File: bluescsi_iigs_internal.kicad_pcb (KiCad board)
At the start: 2 copper layers, 56.6 x 53.3 mm, 16 parts, among them J1 Conn_02x13_Top_Bottom, J2 Conn_02x13_Top_Bottom, J3 Micro_SD_Card, SW1 SW_SPDT, U1 YAAJ_BluePill, U2 UCC5606, U3 UCC5606

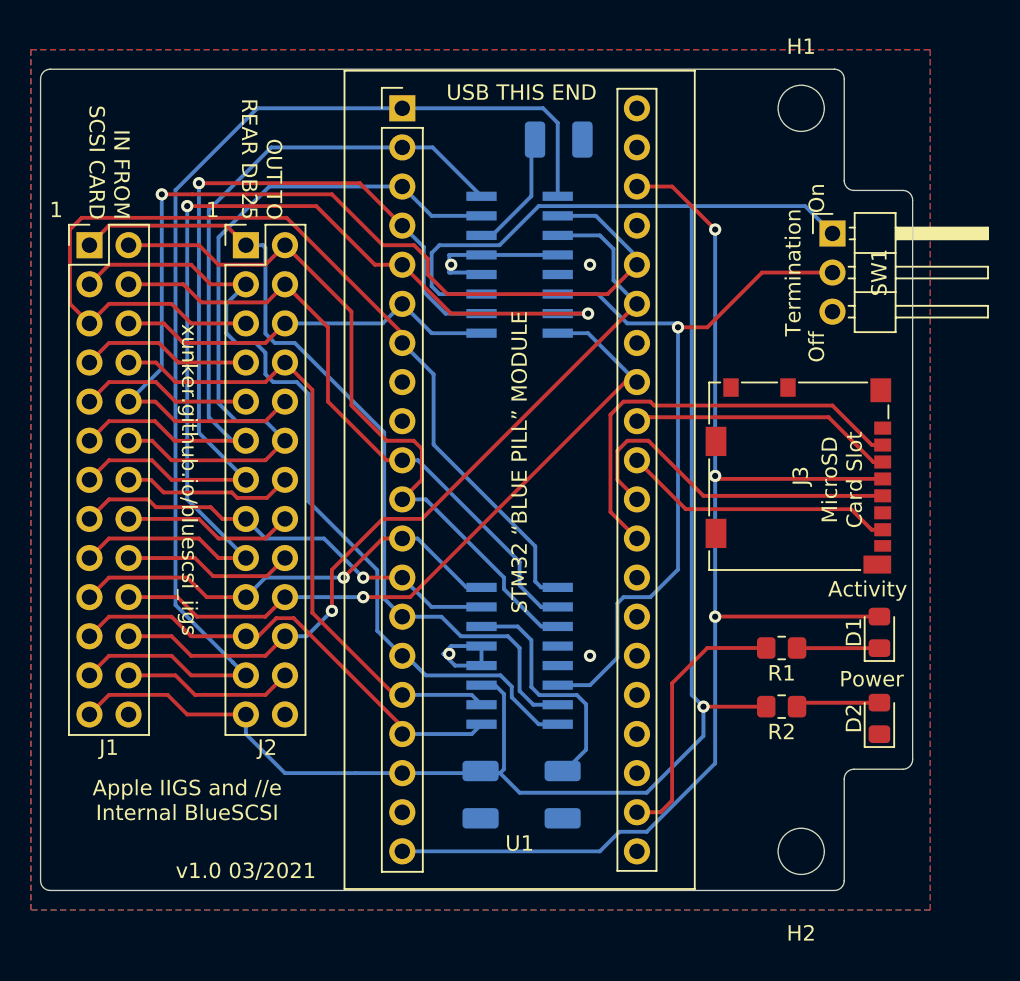
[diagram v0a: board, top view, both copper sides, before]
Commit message: V1.1 from v1.0 Fix IDC26 pin header to be correct! Change capacitor footprint to handsolder variant. Move mounting holes toward centre by about 2.54 and back by 2.54
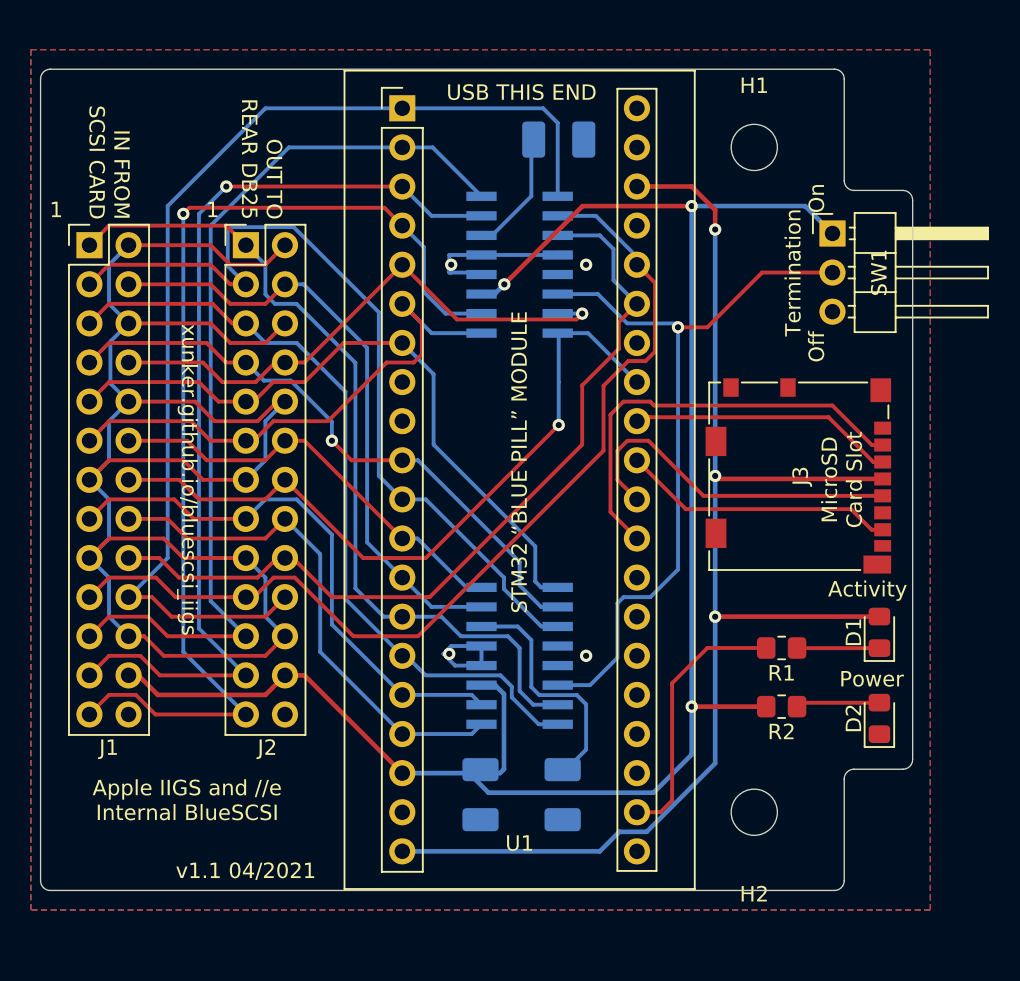
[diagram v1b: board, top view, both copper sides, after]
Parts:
- C1, C2, C3: footprint Capacitor_Tantalum_SMD:CP_EIA-3528-21_Kemet-B -> Capacitor_Tantalum_SMD:CP_EIA-3528-21_Kemet-B_Pad1.50x2.35mm_HandSolder
- J1, J2: value Conn_02x13_Top_Bottom -> Conn_02x13_Odd_Even
- moved H1 3.97 mm to (175.3, 53.3)
- moved H2 3.97 mm to (175.3, 96.5)
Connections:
- J1 pad 10: /SCSI_DB3 -> GND
- J1 pad 11: /SCSI_DB5 -> /SCSI_BSY
- J1 pad 12: /SCSI_DB6 -> /SCSI_SEL
- J1 pad 13: /SCSI_DB7 -> GND
- J1 pad 14: GND -> /SCSI_DBP
- J1 pad 15: /SCSI_C_D -> /SCSI_DB0
- J1 pad 16: GND -> /SCSI_DB1
- J1 pad 17: /SCSI_ATN -> GND
- J1 pad 18: GND -> /SCSI_DB2
- J1 pad 19: /SCSI_SEL -> /SCSI_DB3
- J1 pad 2: /SCSI_MSG -> GND
- J1 pad 20: /SCSI_DBP -> /SCSI_DB4
- J1 pad 21: /SCSI_DB1 -> /SCSI_DB5
- J1 pad 22: /SCSI_DB2 -> GND
- J1 pad 23: /SCSI_DB4 -> /SCSI_DB6
- J1 pad 24: GND -> +5V
- J1 pad 25: +5V -> /SCSI_DB7
- J1 pad 3: /SCSI_I_O -> /SCSI_MSG
- J1 pad 4: /SCSI_RST -> /SCSI_C_D
- J1 pad 5: /SCSI_ACK -> /SCSI_I_O
- J1 pad 6: /SCSI_BSY -> GND
- J1 pad 7: GND -> /SCSI_RST
- J1 pad 8: /SCSI_DB0 -> /SCSI_ATN
- J1 pad 9: GND -> /SCSI_ACK
- J2 pad 10: /SCSI_DB3 -> GND
- J2 pad 11: /SCSI_DB5 -> /SCSI_BSY
- J2 pad 12: /SCSI_DB6 -> /SCSI_SEL
- J2 pad 13: /SCSI_DB7 -> GND
- J2 pad 14: GND -> /SCSI_DBP
- J2 pad 15: /SCSI_C_D -> /SCSI_DB0
- J2 pad 16: GND -> /SCSI_DB1
- J2 pad 17: /SCSI_ATN -> GND
- J2 pad 18: GND -> /SCSI_DB2
- J2 pad 19: /SCSI_SEL -> /SCSI_DB3
- J2 pad 2: /SCSI_MSG -> GND
- J2 pad 20: /SCSI_DBP -> /SCSI_DB4
- J2 pad 21: /SCSI_DB1 -> /SCSI_DB5
- J2 pad 22: /SCSI_DB2 -> GND
- J2 pad 23: /SCSI_DB4 -> /SCSI_DB6
- J2 pad 24: GND -> +5V
- J2 pad 25: +5V -> /SCSI_DB7
- J2 pad 3: /SCSI_I_O -> /SCSI_MSG
- J2 pad 4: /SCSI_RST -> /SCSI_C_D
- J2 pad 5: /SCSI_ACK -> /SCSI_I_O
- J2 pad 6: /SCSI_BSY -> GND
- J2 pad 7: GND -> /SCSI_RST
- J2 pad 8: /SCSI_DB0 -> /SCSI_ATN
- J2 pad 9: GND -> /SCSI_ACK
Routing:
- net GND: track 84.2 -> 127.2 mm
- net /SCSI_ATN: track 67.1 -> 36.9 mm, vias 2 -> 1
- net /SCSI_ACK: track 64.3 -> 44.4 mm
- net /SCSI_DB6: track 46.6 -> 62.3 mm, vias 0 -> 1
- net /SCSI_DB7: track 55.3 -> 69.5 mm
- net /SCSI_DB5: track 48.4 -> 59.8 mm
- net /SCSI_C_D: track 28.9 -> 40.1 mm, vias 1 -> 0
- net +5V: track 126.7 -> 117.2 mm, vias 1 -> 3
- net /SCSI_BSY: track 25.3 -> 34.7 mm
- net /SCSI_MSG: track 46.9 -> 54.2 mm
- net /SCSI_DB4: track 76.8 -> 70.8 mm
- net /SCSI_DB0: track 41.7 -> 36.5 mm
- net /SCSI_DB3: track 67.7 -> 62.9 mm, vias 1 -> 0
- net /SCSI_I_O: track 54.6 -> 50.5 mm
- net /SCSI_DB1: track 30.7 -> 34.2 mm
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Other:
- net class POWER: trace_width 0.25 -> 0.3
- board text added: "v1.1 04/2021"
- board text removed: "v1.0 03/2021"

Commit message: Increase trace size for +3.3v and +5v
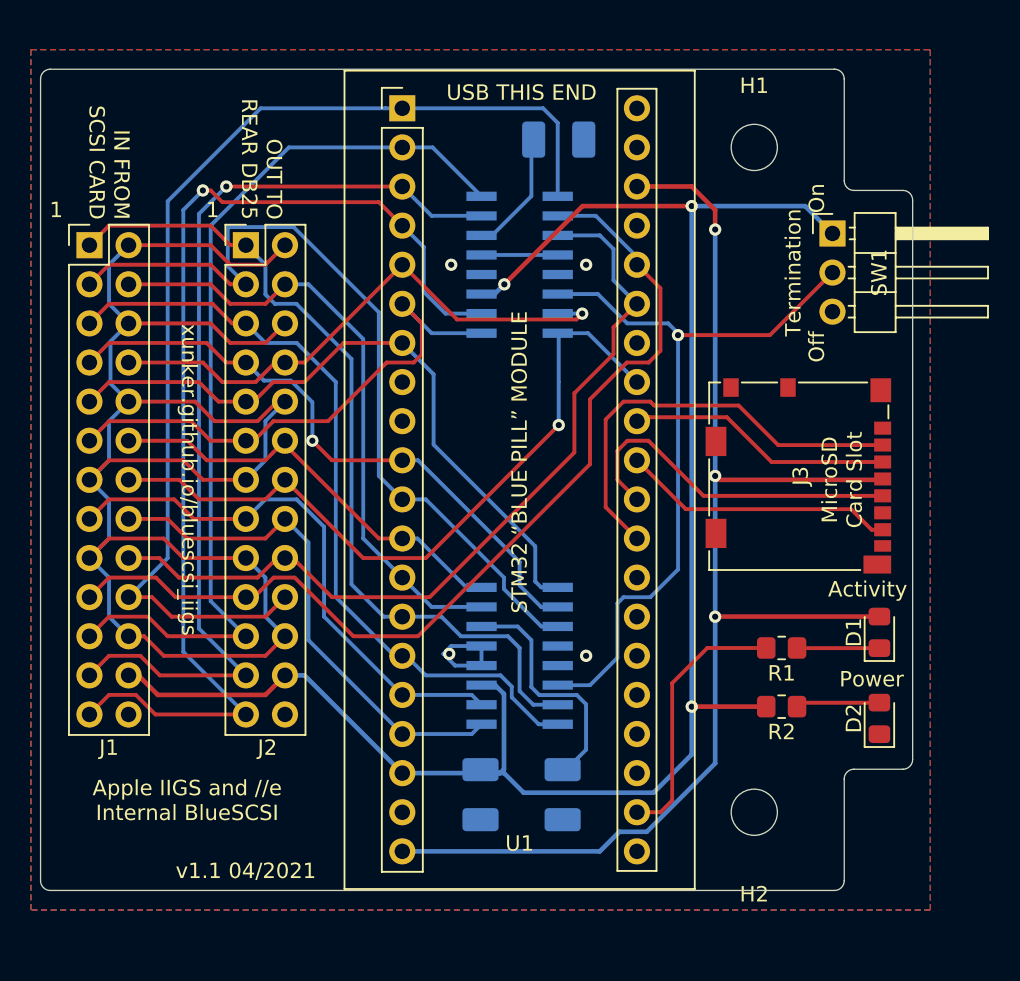
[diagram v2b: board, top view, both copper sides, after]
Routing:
- net GND: track 127.2 -> 122.0 mm
- net /SCSI_DB7: track 69.5 -> 70.6 mm
- net /SCSI_RST: track 39.7 -> 40.4 mm

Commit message: Fix db25 connector wiring
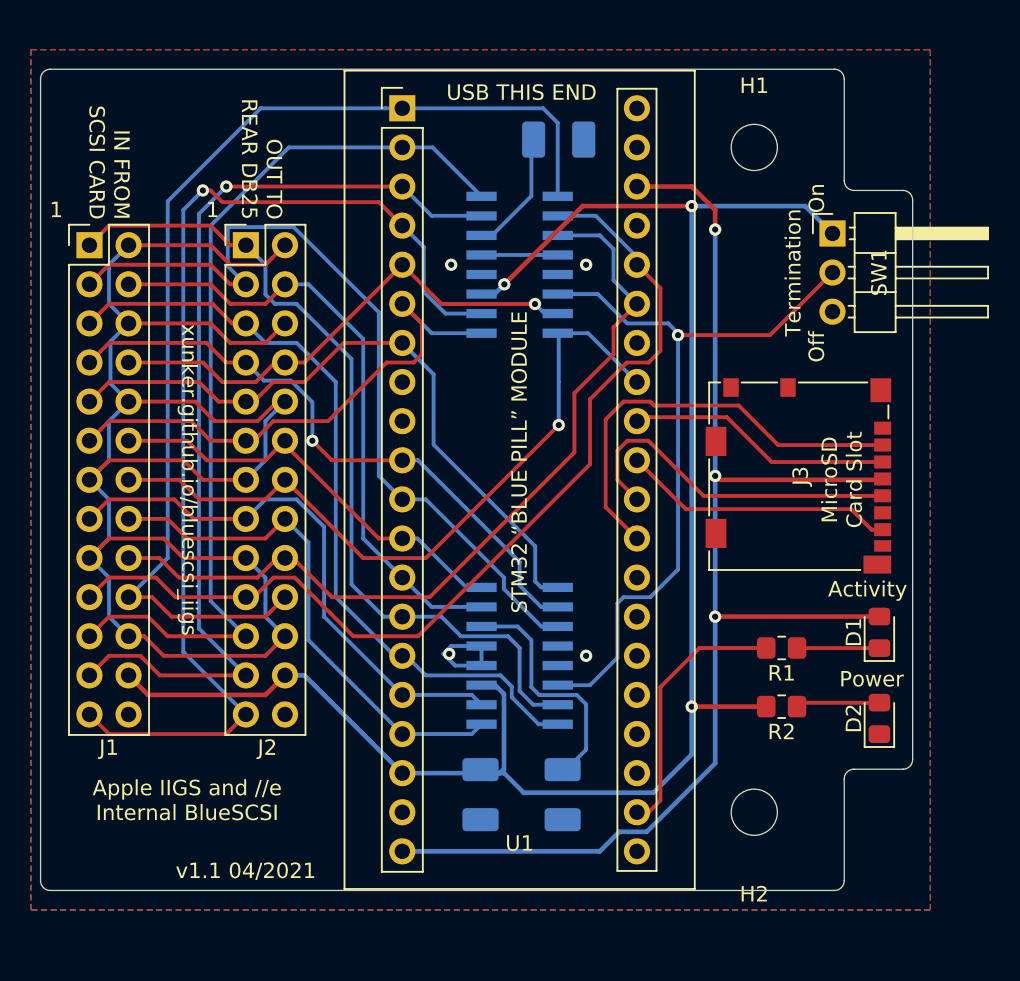
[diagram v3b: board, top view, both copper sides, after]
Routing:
- net /SCSI_ATN: track 36.9 -> 33.4 mm
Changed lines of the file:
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@@
     (thickness 1.6)
     (drawings 46)
-    (tracks 415)
+    (tracks 413)
     (zones 0)
     (modules 16)
@@
   (gr_line (start 180.467 101.6) (end 129.54 101.6) (layer Edge.Cuts) (width 0.05))
   (gr_line (start 185.547 56.769) (end 185.547 93.091) (layer Edge.Cuts) (width 0.05))
-  (segment (start 143.51 88.9) (end 144.78 87.63) (width 0.3) (layer F.Cu) (net 12))
-  (segment (start 135.255 87.63) (end 136.525 88.9) (width 0.3) (layer F.Cu) (net 12))
-  (segment (start 136.525 88.9) (end 143.51 88.9) (width 0.3) (layer F.Cu) (net 12))
-  (segment (start 134.62 87.63) (end 135.255 87.63) (width 0.3) (layer F.Cu) (net 12))
   (segment (start 146.05 87.63) (end 152.4 93.98) (width 0.3) (layer B.Cu) (net 12))
   (segment (start 144.78 87.63) (end 146.05 87.63) (width 0.3) (layer B.Cu) (net 12))
@@
   (via (at 171.196 89.662) (size 0.8) (drill 0.4) (layers F.Cu B.Cu) (net 12))
   (segment (start 176.038 89.662) (end 171.196 89.662) (width 0.3) (layer F.Cu) (net 12))
+  (segment (start 157.545 88.265) (end 158.4265 88.265) (width 0.3) (layer B.Cu) (net 12) (status 30))
+  (segment (start 158.75 93.98) (end 152.4 93.98) (width 0.3) (layer B.Cu) (net 12) (status 20))
+  (segment (start 159.004 93.726) (end 158.75 93.98) (width 0.3) (layer B.Cu) (net 12))
+  (segment (start 159.004 88.8425) (end 159.004 93.726) (width 0.3) (layer B.Cu) (net 12))
+  (segment (start 158.4265 88.265) (end 159.004 88.8425) (width 0.3) (layer B.Cu) (net 12) (status 10))
+  (segment (start 171.196 92.7735) (end 171.196 89.662) (width 0.3) (layer B.Cu) (net 12))
+  (segment (start 168.7195 95.25) (end 171.196 92.7735) (width 0.3) (layer B.Cu) (net 12))
+  (segment (start 160.28075 95.25) (end 168.7195 95.25) (width 0.3) (layer B.Cu) (net 12))
+  (segment (start 158.99725 93.9665) (end 160.28075 95.25) (width 0.3) (layer B.Cu) (net 12))
+  (segment (start 156.718 93.9665) (end 158.99725 93.9665) (width 0.3) (layer B.Cu) (net 12))
+  (segment (start 143.51 88.9) (end 144.78 87.63) (width 0.3) (layer F.Cu) (net 12))
+  (segment (start 135.89 88.9) (end 143.51 88.9) (width 0.3) (layer F.Cu) (net 12))
+  (segment (start 134.62 87.63) (end 135.89 88.9) (width 0.3) (layer F.Cu) (net 12))
   (via (at 155.448 86.233) (size 0.8) (drill 0.4) (layers F.Cu B.Cu) (net 13))
   (segment (start 155.575 85.725) (end 155.067 86.233) (width 0.25) (layer B.Cu) (net 13))
@@
   (segment (start 133.35 63.5) (end 134.62 64.77) (width 0.25) (layer B.Cu) (net 13))
   (segment (start 134.62 59.69) (end 133.35 60.96) (width 0.25) (layer B.Cu) (net 13))
-  (segment (start 157.545 88.265) (end 158.4265 88.265) (width 0.3) (layer B.Cu) (net 12) (status 30))
-  (segment (start 158.75 93.98) (end 152.4 93.98) (width 0.3) (layer B.Cu) (net 12) (status 20))
-  (segment (start 159.004 93.726) (end 158.75 93.98) (width 0.3) (layer B.Cu) (net 12))
-  (segment (start 159.004 88.8425) (end 159.004 93.726) (width 0.3) (layer B.Cu) (net 12))
-  (segment (start 158.4265 88.265) (end 159.004 88.8425) (width 0.3) (layer B.Cu) (net 12) (status 10))
-  (segment (start 171.196 92.7735) (end 171.196 89.662) (width 0.3) (layer B.Cu) (net 12))
-  (segment (start 168.7195 95.25) (end 171.196 92.7735) (width 0.3) (layer B.Cu) (net 12))
-  (segment (start 160.28075 95.25) (end 168.7195 95.25) (width 0.3) (layer B.Cu) (net 12))
-  (segment (start 158.99725 93.9665) (end 160.28075 95.25) (width 0.3) (layer B.Cu) (net 12))
-  (segment (start 156.718 93.9665) (end 158.99725 93.9665) (width 0.3) (layer B.Cu) (net 12))
   (segment (start 162.495 51.751) (end 162.495 56.515) (width 0.25) (layer B.Cu) (net 14) (status 20))
   (segment (start 161.544 50.8) (end 162.495 51.751) (width 0.25) (layer B.Cu) (net 14))
@@
   (segment (start 146.05 67.31) (end 152.4 60.96) (width 0.25) (layer F.Cu) (net 19))
   (segment (start 144.78 67.31) (end 146.05 67.31) (width 0.25) (layer F.Cu) (net 19))
-  (via (at 164.084 64.135) (size 0.8) (drill 0.4) (layers F.Cu B.Cu) (net 19))
-  (segment (start 162.495 64.135) (end 164.084 64.135) (width 0.25) (layer B.Cu) (net 19))
-  (segment (start 163.703 64.516) (end 164.084 64.135) (width 0.25) (layer F.Cu) (net 19))
-  (segment (start 155.956 64.516) (end 163.703 64.516) (width 0.25) (layer F.Cu) (net 19))
-  (segment (start 152.4 60.96) (end 155.956 64.516) (width 0.25) (layer F.Cu) (net 19))
   (segment (start 142.87359 68.58) (end 144.14359 67.31) (width 0.25) (layer F.Cu) (net 19))
   (segment (start 139.446 67.31) (end 140.716 68.58) (width 0.25) (layer F.Cu) (net 19))
@@
   (segment (start 140.716 68.58) (end 142.87359 68.58) (width 0.25) (layer F.Cu) (net 19))
   (segment (start 144.14359 67.31) (end 144.78 67.31) (width 0.25) (layer F.Cu) (net 19))
+  (via (at 161.020008 63.511302) (size 0.8) (drill 0.4) (layers F.Cu B.Cu) (net 19))
+  (segment (start 161.643706 64.135) (end 161.020008 63.511302) (width 0.25) (layer B.Cu) (net 19))
+  (segment (start 152.4 60.96) (end 154.951302 63.511302) (width 0.25) (layer F.Cu) (net 19))
+  (segment (start 162.495 64.135) (end 161.643706 64.135) (width 0.25) (layer B.Cu) (net 19))
+  (segment (start 154.951302 63.511302) (end 161.020008 63.511302) (width 0.25) (layer F.Cu) (net 19))
   (segment (start 154.305 83.185) (end 157.545 83.185) (width 0.25) (layer B.Cu) (net 20) (status 20))
   (segment (start 152.4 81.28) (end 154.305 83.185) (width 0.25) (layer B.Cu) (net 20) (status 10))
@@
   (segment (start 153.797 59.817) (end 153.797 62.7253) (width 0.25) (layer B.Cu) (net 21))
   (segment (start 152.4 58.42) (end 153.797 59.817) (width 0.25) (layer B.Cu) (net 21) (status 10))
-  (segment (start 136.36625 90.17) (end 142.24 90.17) (width 0.25) (layer F.Cu) (net 21))
-  (segment (start 135.09625 88.9) (end 136.36625 90.17) (width 0.25) (layer F.Cu) (net 21))
-  (segment (start 133.35 88.9) (end 135.09625 88.9) (width 0.25) (layer F.Cu) (net 21))
-  (segment (start 132.08 90.17) (end 133.35 88.9) (width 0.25) (layer F.Cu) (net 21))
   (via (at 139.446 56.134) (size 0.8) (drill 0.4) (layers F.Cu B.Cu) (net 21))
   (segment (start 142.24 90.17) (end 138.176 86.106) (width 0.25) (layer B.Cu) (net 21))
@@
   (segment (start 150.876 56.896) (end 140.716 56.896) (width 0.25) (layer F.Cu) (net 21))
   (segment (start 152.4 58.42) (end 150.876 56.896) (width 0.25) (layer F.Cu) (net 21))
+  (segment (start 140.97 91.44) (end 142.24 90.17) (width 0.25) (layer F.Cu) (net 21))
+  (segment (start 133.35 91.44) (end 140.97 91.44) (width 0.25) (layer F.Cu) (net 21))
+  (segment (start 132.08 90.17) (end 133.35 91.44) (width 0.25) (layer F.Cu) (net 21))
   (segment (start 154.305 57.785) (end 157.545 57.785) (width 0.25) (layer B.Cu) (net 22) (status 20))
   (segment (start 152.4 55.88) (end 154.305 57.785) (width 0.25) (layer B.Cu) (net 22) (status 10))
-  (segment (start 133.35 86.36) (end 135.382 86.36) (width 0.25) (layer F.Cu) (net 22))
-  (segment (start 136.652 87.63) (end 142.24 87.63) (width 0.25) (layer F.Cu) (net 22))
-  (segment (start 135.382 86.36) (end 136.652 87.63) (width 0.25) (layer F.Cu) (net 22))
-  (segment (start 132.08 87.63) (end 133.35 86.36) (width 0.25) (layer F.Cu) (net 22))
   (via (at 140.969994 55.88) (size 0.8) (drill 0.4) (layers F.Cu B.Cu) (net 22))
   (segment (start 152.4 55.88) (end 140.969994 55.88) (width 0.25) (layer F.Cu) (net 22))
@@
   (segment (start 139.192 84.582) (end 139.192 57.657994) (width 0.25) (layer B.Cu) (net 22))
   (segment (start 139.192 57.657994) (end 140.969994 55.88) (width 0.25) (layer B.Cu) (net 22))
+  (segment (start 136.652 87.63) (end 142.24 87.63) (width 0.25) (layer F.Cu) (net 22))
+  (segment (start 135.382 86.36) (end 136.652 87.63) (width 0.25) (layer F.Cu) (net 22))
+  (segment (start 133.35 86.36) (end 135.382 86.36) (width 0.25) (layer F.Cu) (net 22))
+  (segment (start 132.08 87.63) (end 133.35 86.36) (width 0.25) (layer F.Cu) (net 22))
   (segment (start 154.37 53.34) (end 157.545 56.515) (width 0.25) (layer B.Cu) (net 23) (status 20))
   (segment (start 152.4 53.34) (end 154.37 53.34) (width 0.25) (layer B.Cu) (net 23) (status 10))
@@
   (segment (start 167.64 78.74) (end 165.608 76.708) (width 0.25) (layer F.Cu) (net 36))
   (segment (start 178.308 89.408) (end 183.871 89.408) (width 0.25) (layer F.Cu) (net 39) (status 30))
-  (segment (start 176.038 85.852) (end 172.212 85.852) (width 0.25) (layer F.Cu) (net 40) (status 10))
-  (segment (start 172.212 85.852) (end 169.926 88.138) (width 0.25) (layer F.Cu) (net 40))
-  (segment (start 169.164 96.52) (end 167.64 96.52) (width 0.25) (layer F.Cu) (net 40) (status 20))
-  (segment (start 169.926 88.138) (end 169.926 95.758) (width 0.25) (layer F.Cu) (net 40))
-  (segment (start 169.926 95.758) (end 169.164 96.52) (width 0.25) (layer F.Cu) (net 40))
+  (segment (start 168.402 96.52) (end 167.64 96.52) (width 0.25) (layer F.Cu) (net 40))
+  (segment (start 169.164 88.392) (end 169.164 95.758) (width 0.25) (layer F.Cu) (net 40))
+  (segment (start 171.704 85.852) (end 169.164 88.392) (width 0.25) (layer F.Cu) (net 40))
+  (segment (start 169.164 95.758) (end 168.402 96.52) (width 0.25) (layer F.Cu) (net 40))
+  (segment (start 176.038 85.852) (end 171.704 85.852) (width 0.25) (layer F.Cu) (net 40))
   (segment (start 157.545 59.055) (end 158.23 59.055) (width 0.25) (layer B.Cu) (net 41) (status 30))
   (segment (start 160.782 56.503) (end 160.782 53.768) (width 0.25) (layer B.Cu) (net 41) (status 20))
